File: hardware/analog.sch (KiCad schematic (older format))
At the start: 23 parts, among them U4 LTC6257

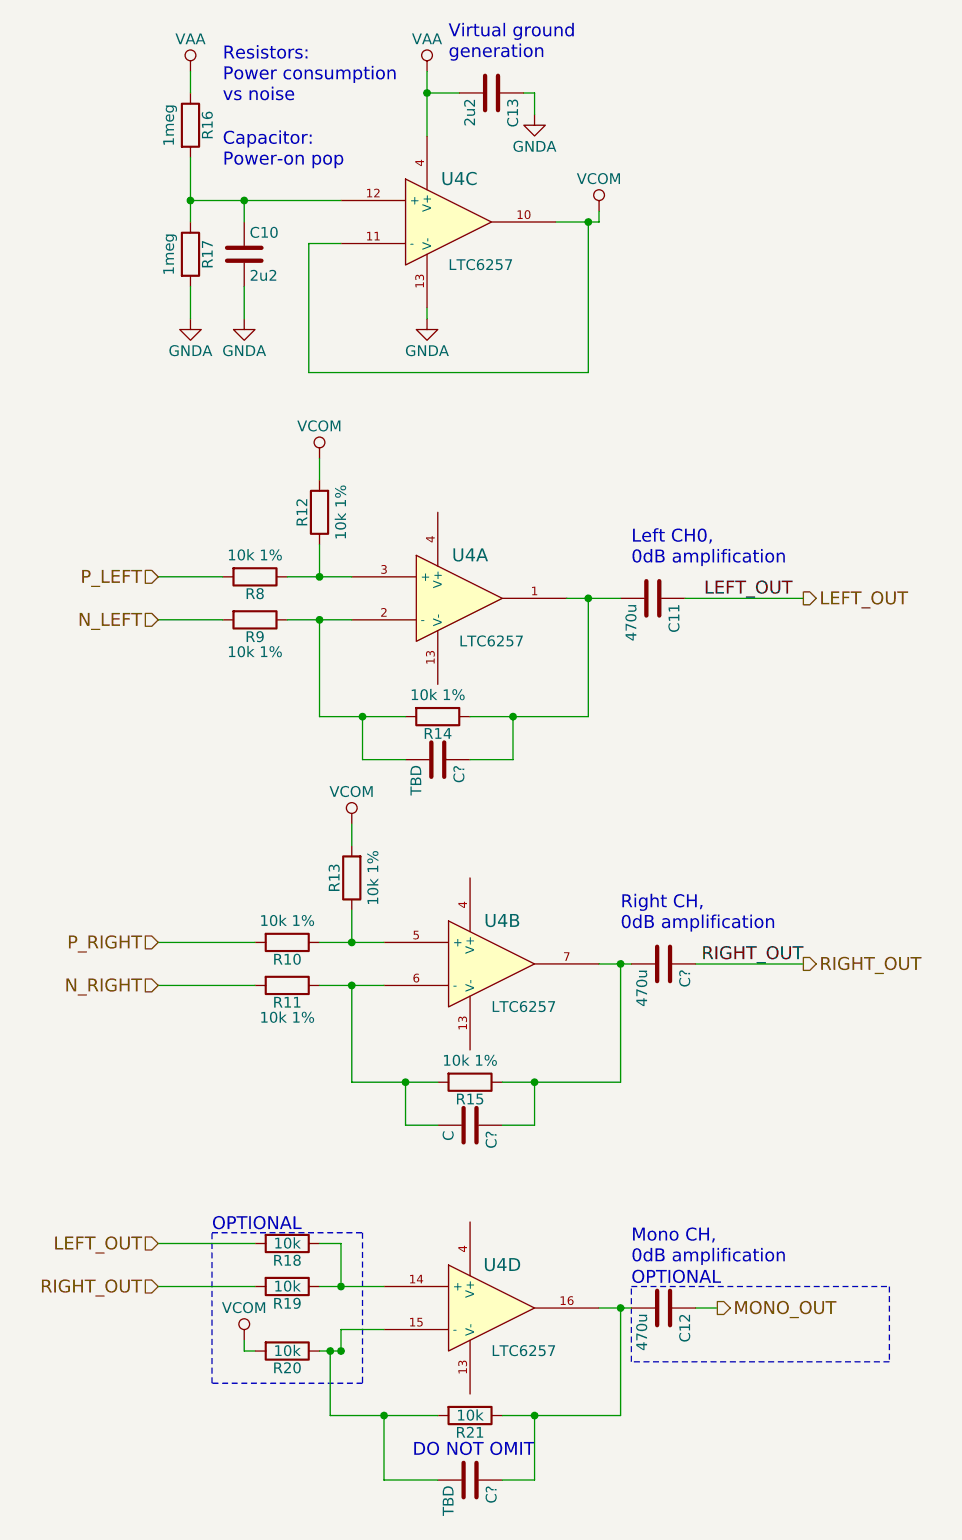
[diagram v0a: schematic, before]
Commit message: Add user IO, programming headers
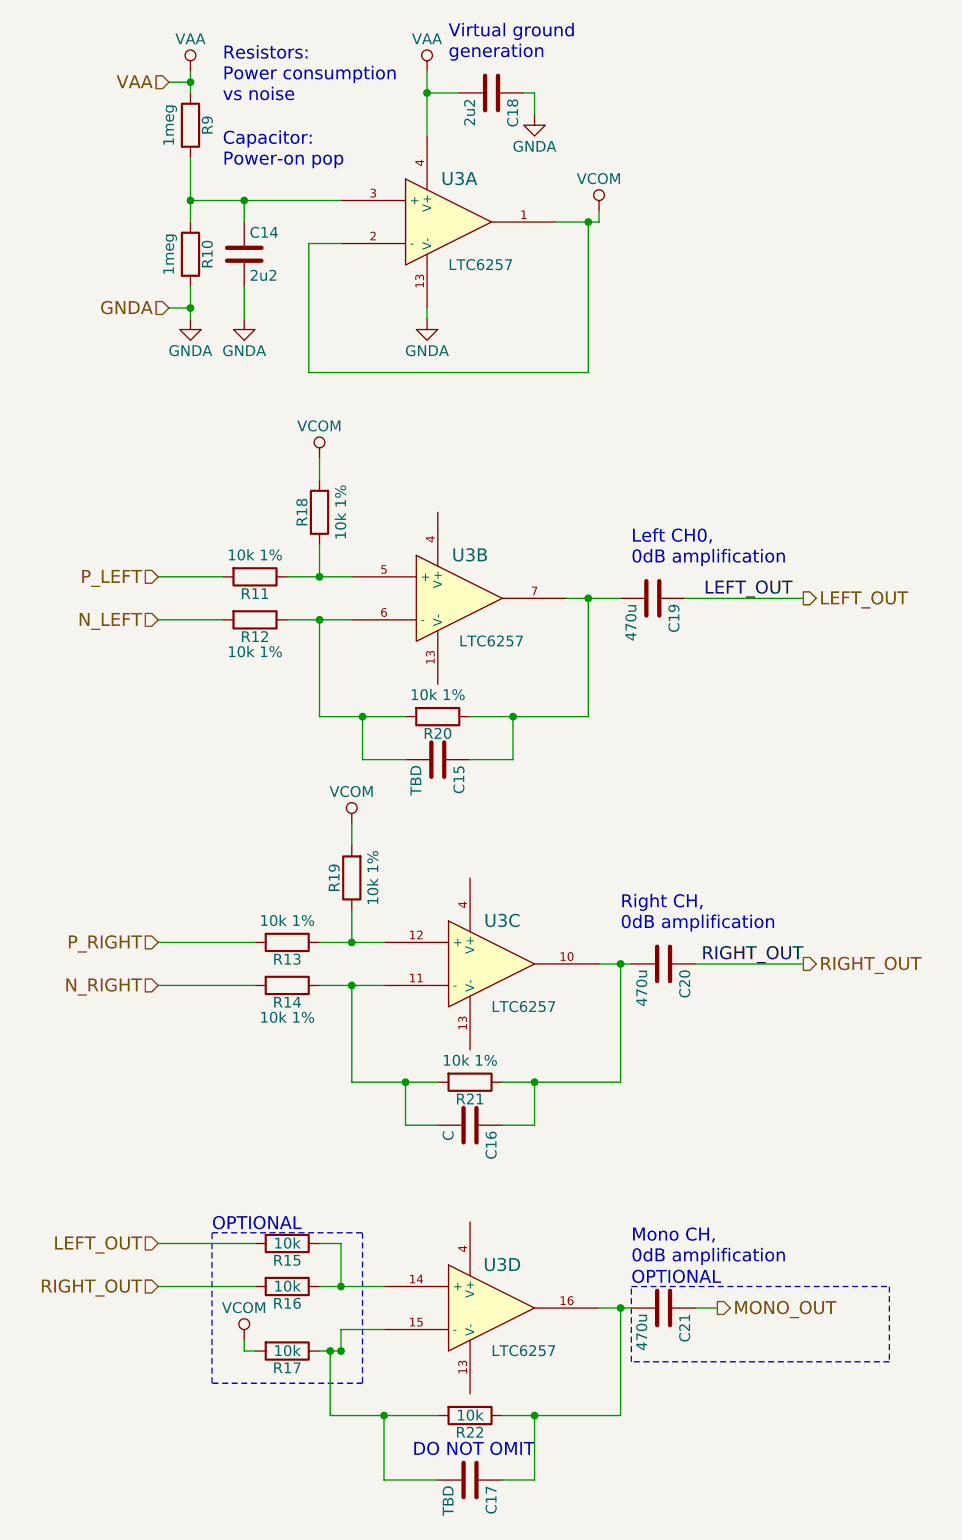
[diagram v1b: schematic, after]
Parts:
- gave numbers to parts that had none: 4
- renumbered C10 to C14, C13 to C18, C11 to C19, C12 to C21, R17 to R10, R8 to R11, R9 to R12, R10 to R13, R11 to R14, R18 to R15, R19 to R16, R20 to R17, R12 to R18, R13 to R19, R14 to R20, R15 to R21, R21 to R22, R16 to R9, U4 to U3
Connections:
- net VCOM: now also U3.1, U3.2 (-); no longer U3.10, U3.11 (-)
- net at C15.1, C19.2, R20.1: now also U3.7; no longer U3.1
- net at C15.2, R12.1, R20.2: now also U3.6 (-); no longer U3.2 (-)
- net at R11.1, R18.1: now also U3.5 (+); no longer U3.3 (+)
- net at C14.1, R10.1, R9.2: now also U3.3 (+); no longer U3.12 (+)
- net at R13.1, R19.1: now also U3.12 (+); no longer U3.5 (+)
- net at C16.2, R14.1, R21.2: now also U3.11 (-); no longer U3.6 (-)
- net at C16.1, C20.2, R21.1: now also U3.10; no longer U3.7
